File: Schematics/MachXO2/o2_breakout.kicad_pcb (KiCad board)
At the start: 2 copper layers, 95 x 72 mm, 104 parts, among them J1 Conn_02x20_Odd_Even, J2 Conn_02x20_Odd_Even, J3 USB_B_Micro, J4 DM3AT-SF-PEJM5, SW1 USER, SW2 Reset, U1 LCMXO2-2000HC-4TG100C, U2 FT2232D, U3 TCM809, U4 93C56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

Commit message: BUG Fix.
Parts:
- moved R24 2.57 mm to (163.9, 102.6), turned to 90 degrees
- moved C36 0.43 mm to (114.7, 118.0)
- moved R21 0.18 mm to (166.6, 106.8)
- moved R22 0.09 mm to (166.6, 107.9)
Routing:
- net /JTAG_TCK: track 87.7 -> 88.6 mm
- net GND: vias 227 -> 228

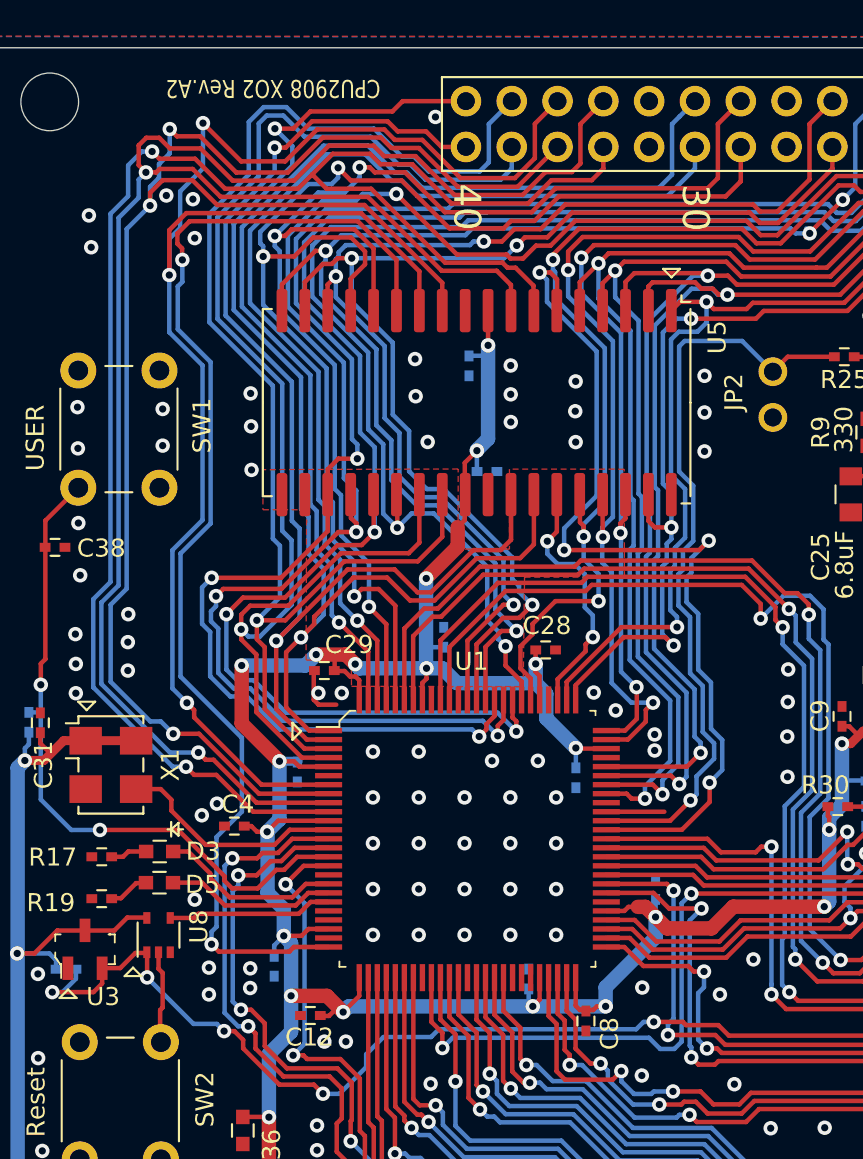
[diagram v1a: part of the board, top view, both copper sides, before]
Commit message: Add .dw directive.
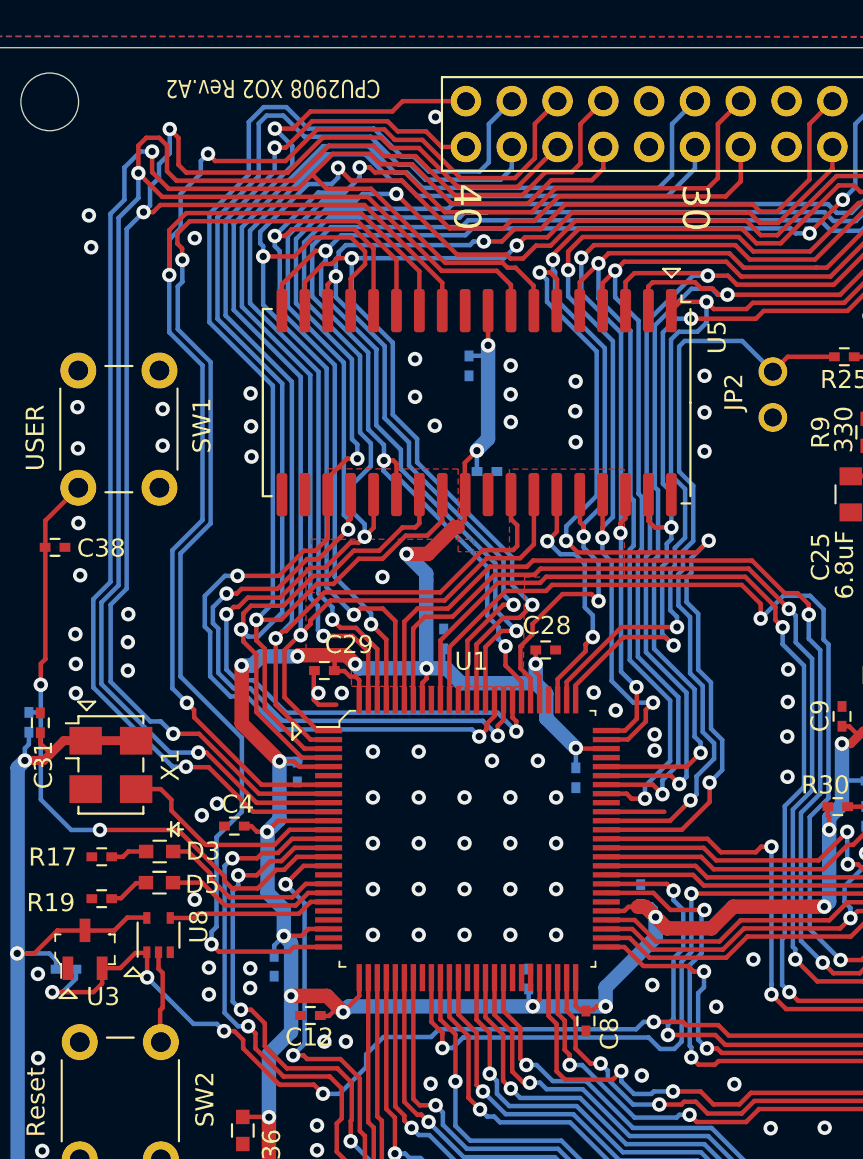
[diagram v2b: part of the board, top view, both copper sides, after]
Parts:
- moved C2 0.87 mm to (136.8, 105.0)
- moved C1 0.09 mm to (125.8, 90.8)
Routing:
- net /IO3: track 90.6 -> 88.1 mm
- net /IO7: track 70.4 -> 68.0 mm
- net +3V3: track 470.0 -> 472.2 mm
- net /A9: track 76.0 -> 74.0 mm
- net /A11: track 96.9 -> 95.2 mm
- net /A19: track 60.7 -> 61.7 mm
- net /IO6: track 69.0 -> 68.2 mm
- net /IO5: track 74.4 -> 73.6 mm
- net /IO1: track 103.5 -> 104.2 mm
- net /IO0: track 92.5 -> 93.2 mm
- net /A13: track 73.4 -> 72.7 mm
- net /A15: track 65.6 -> 64.9 mm
- net /A14: track 65.8 -> 65.3 mm
- net /A12: track 86.9 -> 86.4 mm
- net /A18: track 58.2 -> 58.7 mm
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
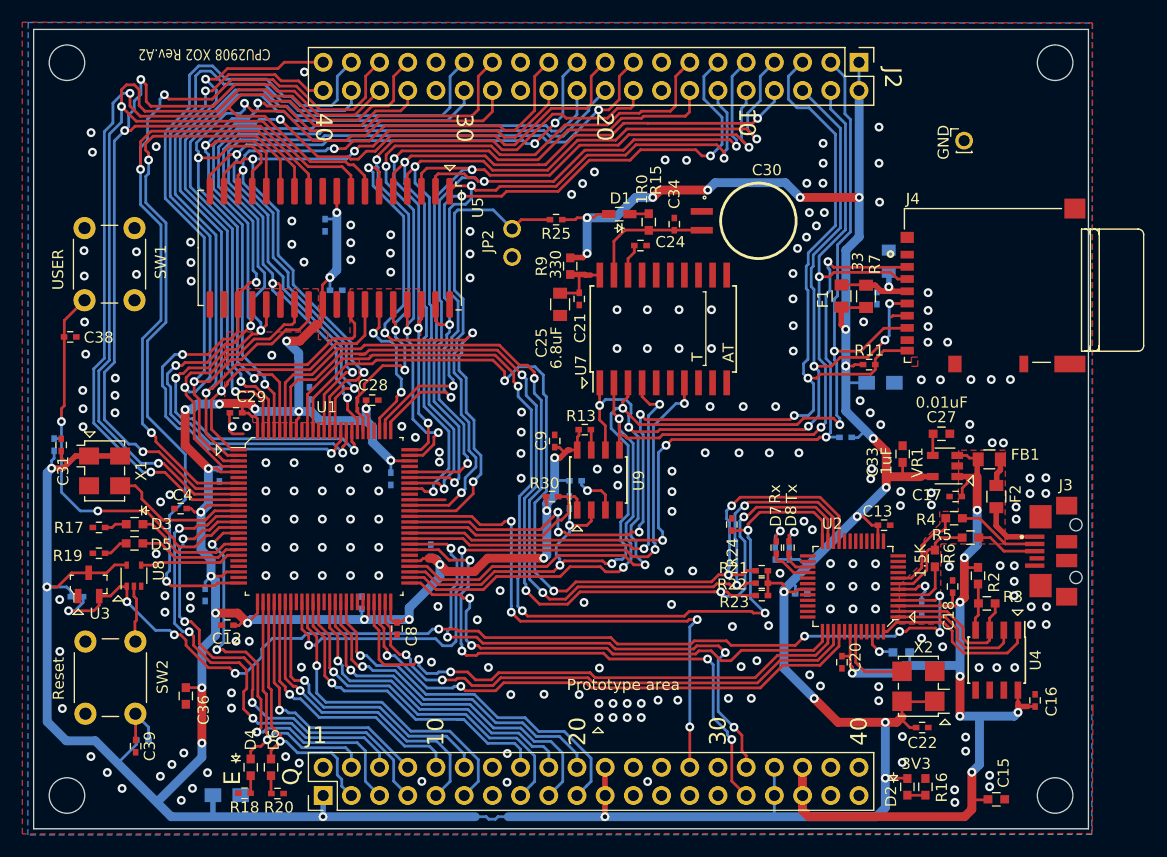
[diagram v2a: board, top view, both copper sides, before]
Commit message: asq bug fix.
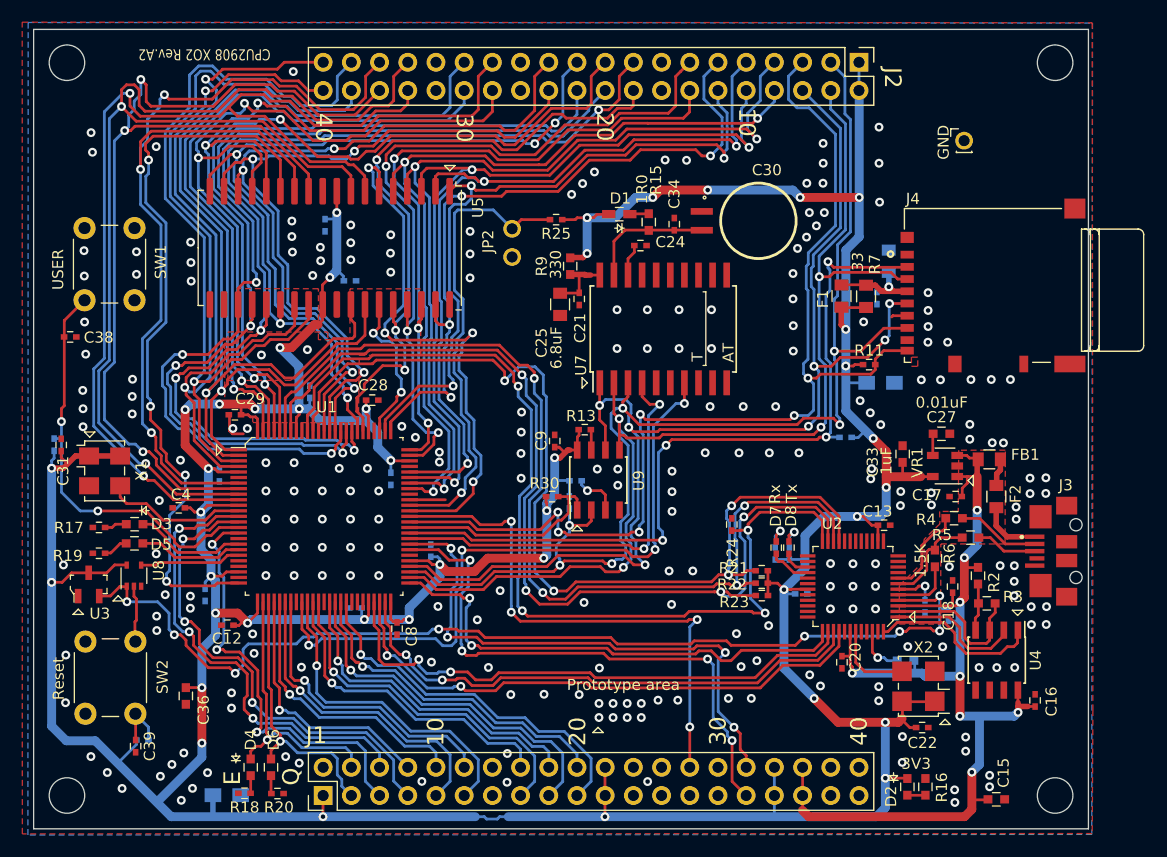
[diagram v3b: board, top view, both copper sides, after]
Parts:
- moved R12 78.5 mm to (183.4, 110.7), turned to 90 degrees
- moved C7 1.51 mm to (129.5, 80.6)
- moved R1 0.84 mm to (179.5, 114.9)
- moved C10 0.74 mm to (130.0, 110.1), turned to 180 degrees
- moved C14 0.30 mm to (181.3, 110.0)
- moved C29 0.20 mm to (119.1, 92.7)
- moved C4 0.18 mm to (114.1, 101.1)
- moved C1 0.14 mm to (125.9, 90.6)
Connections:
- R12 pad 1: +3V3 -> +5V
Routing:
- net /FT_Reset: track 97.3 -> 93.2 mm, vias 9 -> 8
- net +3V3: track 472.2 -> 469.7 mm
- net /IO7: track 68.0 -> 69.6 mm
- net /A10: track 91.6 -> 90.0 mm
- net /A14: track 65.3 -> 66.7 mm
- net /A13: track 72.7 -> 74.0 mm
- net /A15: track 64.9 -> 66.2 mm
- net /IO6: track 68.2 -> 69.4 mm
- net +5V: track 90.4 -> 91.6 mm
- net Net-(R1-Pad2): track 3.30 -> 4.37 mm
- net /A9: track 74.0 -> 74.8 mm
- net /IO3: track 88.1 -> 88.9 mm
- net /JTAG_TDO: track 89.0 -> 88.2 mm
- net /IO4: track 75.3 -> 74.5 mm
- net /JTAG_TDI: track 89.2 -> 88.6 mm
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
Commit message: Clean up.
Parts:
- C23: footprint Capacitors_SMD:C_0805 -> Capacitors_SMD:C_1210
- R15: value 1R0 -> 33
- moved C2 1.49 mm to (135.9, 106.2), turned to 180 degrees
- moved C23 0.98 mm to (178.1, 77.9)
- moved C10 0.28 mm to (130.0, 109.8)
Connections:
- net Net-(C21-Pad1) renamed /SDCARD/RTCVdd
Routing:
- net +3V3: track 469.7 -> 471.0 mm, vias 41 -> 40
- net /SPI_CS1: track 71.6 -> 70.4 mm
- net /~SD_CD: track 96.8 -> 97.8 mm
- net /A0: track 75.0 -> 76.0 mm
- net /SDCARD/VddSD: track 9.54 -> 10.4 mm
- net /SPI_MISO: track 110.0 -> 110.8 mm
- net /IO2: track 93.7 -> 94.4 mm
- net /SPI_CLK: track 110.6 -> 111.1 mm
- net /GCLK1: track 48.5 -> 49.1 mm

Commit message: PCB RevA3.
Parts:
- moved H5 8.26 mm to (193.1, 67.9)
- moved C1 3.45 mm to (123.5, 93.2), turned to 180 degrees
- moved R14 1.38 mm to (149.7, 100.0)
- moved C11 1.14 mm to (171.0, 108.2)
- moved C38 0.95 mm to (104.8, 86.5), turned to 270 degrees
- moved R8 0.89 mm to (148.8, 101.3), turned to 0 degrees
- moved C2 0.80 mm to (135.5, 106.9)
- moved SW1 0.68 mm to (110.2, 76.6)
- moved R24 0.60 mm to (163.4, 102.2), turned to 180 degrees
- moved C23 0.30 mm to (178.0, 78.2)
- moved R1 0.10 mm to (179.5, 115.0)
- moved C5 0.05 mm to (117.7, 98.1)
- turned R12 to 270 degrees
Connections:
- net Net-(R13-Pad2) renamed /SDCARD/~HOLD
- net Net-(R14-Pad2) renamed /SDCARD/~WP
- J1 pad 27: Net-(J1-Pad27) -> /~CS2
- J1 pad 29: Net-(J1-Pad29) -> GND
- U1 pad 61: /SPI_CS0 -> /~SD_CD
- U1 pad 62: /~SD_CD -> /SPI_CS0
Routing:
- net /~CS2: track 3.26 -> 56.6 mm, vias 0 -> 5
- net /IO3: track 88.9 -> 95.4 mm, vias 3 -> 2
- net /~SD_CD: track 97.8 -> 93.2 mm, vias 6 -> 4
- net +3V3: track 471.0 -> 468.5 mm, vias 40 -> 41
- net /IO6: track 69.4 -> 71.8 mm
- net /SPI_CS0: track 19.7 -> 17.6 mm
- net /IO5: track 73.7 -> 71.9 mm
- net /SPI_CLK: track 111.1 -> 112.6 mm
- net GND: track 4.31 -> 2.87 mm, vias 229 -> 239
- net /FT_Reset: track 93.2 -> 94.6 mm
- net /IO2: track 94.4 -> 93.0 mm
- net /A17: track 71.3 -> 72.6 mm
- net /SPI_CS3: track 49.9 -> 51.2 mm, vias 4 -> 3
- net /JTAG_TCK: track 88.6 -> 87.4 mm
- net /IO0: track 93.4 -> 94.5 mm
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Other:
- board text added: "CPU2908 XO2 Rev.A3"
- board text removed: "CPU2908 XO2 Rev.A2"

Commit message: revA3
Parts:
- removed D1: D, Capacitors_SMD:C_0603_HandSoldering
- removed D4, D6: LED, Capacitors_SMD:C_0603
- removed R20: 47K, Capacitors_SMD:C_0402
- added C26: 0.1uF, Capacitors_SMD:C_0402, F.Cu at (105.8, 91.2)
- added D10: LED, Capacitors_SMD:C_0603, F.Cu at (143.6, 73.9)
- added D9: LED, Capacitors_SMD:C_0603, F.Cu at (177.7, 71.7)
- added R31: 47K, Capacitors_SMD:C_0402, B.Cu at (182.4, 73.1)
- added R32: 47K, Capacitors_SMD:C_0402, F.Cu at (146.7, 74.0)
- added SW3: SW_Push, digikey-footprints:SMD-2_3.2x1.5mm, F.Cu at (106.9, 89.1)
- added U6: MAX40200AUK, TO_SOT_Packages_SMD:SOT-23-5, F.Cu at (153.5, 74.8)
- C23, C3, C37: moved to F.Cu
- C24: moved to B.Cu
- R18: value 47K -> 10K; moved to B.Cu
- moved R18 29.8 mm to (103.7, 101.8), turned to 270 degrees
- moved C19 23.1 mm to (104.4, 108.6), turned to 90 degrees
- moved C23 9.89 mm to (168.8, 81.9), turned to 180 degrees
- moved C31 6.02 mm to (109.4, 94.3), turned to 0 degrees
- moved R19 2.40 mm to (104.7, 104.3)
- moved R17 2.25 mm to (104.6, 103.0)
- moved D3 2.25 mm to (107.9, 102.7)
- moved D5 2.25 mm to (107.8, 104.4)
- moved C3 1.66 mm to (116.0, 107.3), turned to 180 degrees
- moved R7 1.37 mm to (174.6, 82.1)
- moved F1 1.35 mm to (172.5, 82.5)
- moved R29 1.30 mm to (174.2, 93.4)
- moved C20 1.25 mm to (173.9, 116.2)
- moved C34 1.18 mm to (158.5, 74.4), turned to 270 degrees
- moved C10 1.10 mm to (131.1, 109.8), turned to 0 degrees
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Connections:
- C34 pad 1: /SDCARD/VBat -> Net-(C34-Pad1)
- R15 pad 1: Net-(D1-Pad1) -> Net-(C34-Pad1)
- R18 pad 1: Net-(D4-Pad1) -> +3V3
- R18 pad 2: GND -> /INT
- U1 pad 21: Net-(U1-Pad21) -> /INT
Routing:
- net /INT: track 0.00 -> 38.3 mm, vias 0 -> 4
- net /~CE: track 50.3 -> 65.4 mm, vias 4 -> 5
- net +3V3: track 468.5 -> 476.4 mm
- net /SPI_CS1: track 69.9 -> 77.6 mm, vias 4 -> 5
- net Net-(C34-Pad1): track 0.00 -> 4.91 mm
- net Net-(D9-Pad1): track 0.00 -> 4.49 mm, vias 0 -> 1
- net /~CS2: track 56.6 -> 52.8 mm
- net /A16: track 73.7 -> 71.1 mm
- net /IO0: track 94.5 -> 92.0 mm
- net /clkE: track 25.1 -> 23.0 mm
- net /SPI_MISO: track 111.2 -> 109.1 mm
- net /USER_LED1: track 10.1 -> 12.2 mm
- net Net-(D1-Pad1): track 2.05 -> 0.00 mm
- net /USER_LED2: track 9.44 -> 11.3 mm
- net /~TSC: track 38.6 -> 40.4 mm
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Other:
- board text added: "XO2 Rev.A3"
- board text added: "http://2908.work"
- board text added: "~CS0"
- board text added: "~SPICS1"
- board text removed: "CPU2908 XO2 Rev.A3"
- board text removed: "E"
- board text removed: "Q"

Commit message: Update Gerber Data to RevA5
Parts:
- moved C14 2.58 mm to (179.6, 108.0), turned to 180 degrees
- moved C12 2.14 mm to (120.1, 112.4)
- moved C18 1.03 mm to (183.9, 109.2)
- moved R12 0.79 mm to (183.3, 111.5), turned to 90 degrees
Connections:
- R12 pad 2: /FT_Reset -> /FT2232D/~RESET
- U2 pad 4: /FT_Reset -> /FT2232D/~RESET
- U3 pad 2: /FT_Reset -> Net-(U3-Pad2)
- U8 pad 1: /FT_Reset -> Net-(U3-Pad2)
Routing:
- net /FT_Reset: track 94.1 -> 0.00 mm, vias 8 -> 0
- net /A13: track 73.3 -> 80.2 mm, vias 4 -> 2
- net /FT2232D/~RESET: track 0.00 -> 5.66 mm, vias 0 -> 1
- net Net-(U3-Pad2): track 0.00 -> 2.50 mm
- net +5V: track 93.6 -> 94.5 mm
- net GND: vias 251 -> 249
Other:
- board text added: "XO2 Rev.A5"
- board text removed: "XO2 Rev.A3"

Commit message: インストラクション変更
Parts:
- C4: moved to B.Cu
- moved C4 4.56 mm to (118.1, 101.5), turned to 270 degrees
- moved C22 0.28 mm to (180.8, 120.8)
- moved C18 0.06 mm to (184.0, 109.2)
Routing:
- net +3V3: track 475.9 -> 474.7 mm
- net /JTAG_TCK: track 86.7 -> 87.4 mm
- net GND: vias 249 -> 252
